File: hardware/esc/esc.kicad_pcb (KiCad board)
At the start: 6 copper layers, 38 x 41.5 mm, 225 parts, among them J1 TO_FC, J10 PHASE_A, J11 PHASE_B, J12 PHASE_C, J13 PHASE_A, J14 PHASE_B, J15 PHASE_C, J2 BAT_IN, J3 BAT_GND, J4 PHASE_A, J5 PHASE_B, J6 PHASE_C, J7 PHASE_A, J8 PHASE_B, J9 PHASE_C, Q1 NVTFWS003N04XMTAG, Q10 NVTFWS003N04XMTAG, Q11 NVTFWS003N04XMTAG, Q12 NVTFWS003N04XMTAG, Q13 NVTFWS003N04XMTAG, Q14 NVTFWS003N04XMTAG, Q15 NVTFWS003N04XMTAG, Q16 NVTFWS003N04XMTAG, Q17 NVTFWS003N04XMTAG, Q18 NVTFWS003N04XMTAG, Q19 NVTFWS003N04XMTAG, Q2 NVTFWS003N04XMTAG, Q20 NVTFWS003N04XMTAG, Q21 NVTFWS003N04XMTAG, Q22 NVTFWS003N04XMTAG, Q23 NVTFWS003N04XMTAG, Q24 NVTFWS003N04XMTAG, Q3 NVTFWS003N04XMTAG, Q4 NVTFWS003N04XMTAG, Q5 NVTFWS003N04XMTAG, Q6 NVTFWS003N04XMTAG, Q7 NVTFWS003N04XMTAG, Q8 NVTFWS003N04XMTAG, Q9 NVTFWS003N04XMTAG, U1 DRV8300DRGER, U10 DRV8300DRGER, U11 STM32G071K8U6, U12 INA180A1, U13 TPS56339DDC, U14 NCP59800BMNADJTAG, U2 NCP59800BMNADJTAG, U2 STM32G071K8U6, U3 INA180A1, U4 DRV8300DRGER, U5 STM32G071K8U6, U6 INA180A1, U7 DRV8300DRGER, U8 STM32G071K8U6, U9 INA180A1

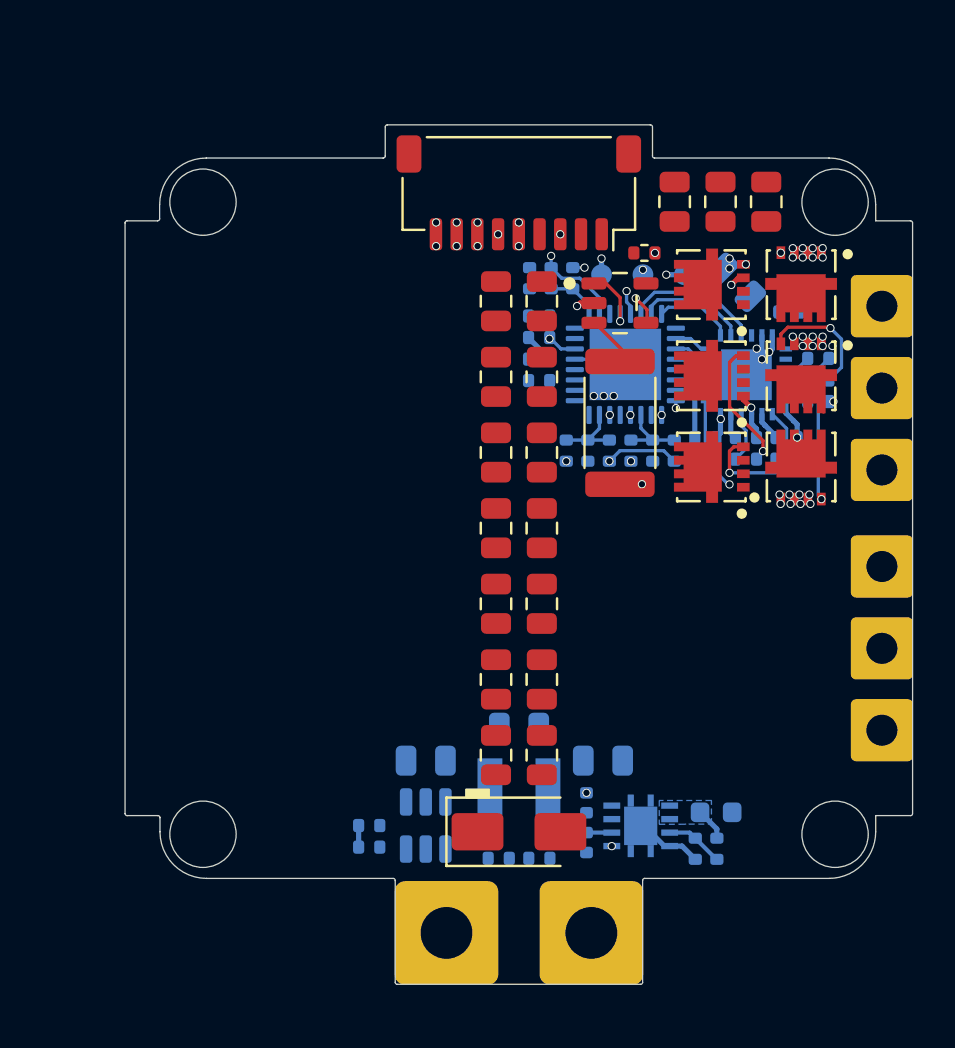
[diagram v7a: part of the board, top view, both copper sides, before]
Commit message: h/fix: edge cuts
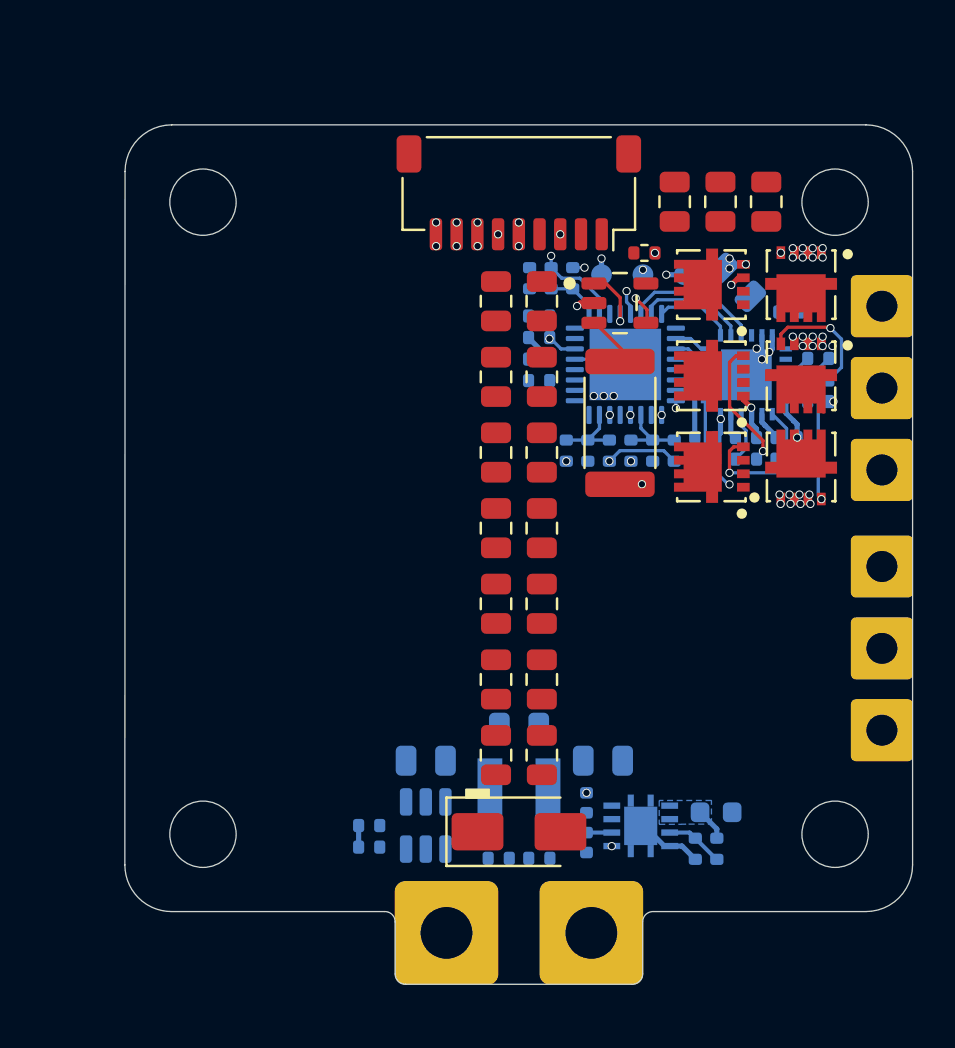
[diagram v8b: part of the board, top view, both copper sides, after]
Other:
- outline, holes or cut-outs redrawn
